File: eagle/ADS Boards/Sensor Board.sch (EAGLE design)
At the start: 15 parts

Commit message: Finish Preliminary Board Layouts
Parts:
- added H1, H2, H3, H4: MOUNT-HOLE3.0, holes:MOUNT-HOLE3.0
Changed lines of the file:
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@@
 <attribute name="DESIGNER" value="Yichen Xu"/>
 </part>
+<part name="H1" library="holes" library_urn="urn:adsk.eagle:library:237" deviceset="MOUNT-HOLE" device="3.0" package3d_urn="urn:adsk.eagle:package:14277/1"/>
+<part name="H2" library="holes" library_urn="urn:adsk.eagle:library:237" deviceset="MOUNT-HOLE" device="3.0" package3d_urn="urn:adsk.eagle:package:14277/1"/>
+<part name="H3" library="holes" library_urn="urn:adsk.eagle:library:237" deviceset="MOUNT-HOLE" device="3.0" package3d_urn="urn:adsk.eagle:package:14277/1"/>
+<part name="H4" library="holes" library_urn="urn:adsk.eagle:library:237" deviceset="MOUNT-HOLE" device="3.0" package3d_urn="urn:adsk.eagle:package:14277/1"/>
 </parts>
 <sheets>
@@
 <attribute name="CREVISION" x="234.92" y="1.17" size="2.54" layer="94" font="vector"/>
 </instance>
+<instance part="H1" gate="G$1" x="226.06" y="144.78" smashed="yes">
+<attribute name="NAME" x="228.092" y="145.3642" size="1.778" layer="95"/>
+<attribute name="VALUE" x="228.092" y="142.3162" size="1.778" layer="96"/>
+</instance>
+<instance part="H2" gate="G$1" x="226.06" y="137.16" smashed="yes">
+<attribute name="NAME" x="228.092" y="137.7442" size="1.778" layer="95"/>
+<attribute name="VALUE" x="228.092" y="134.6962" size="1.778" layer="96"/>
+</instance>
+<instance part="H3" gate="G$1" x="226.06" y="129.54" smashed="yes">
+<attribute name="NAME" x="228.092" y="130.1242" size="1.778" layer="95"/>
+<attribute name="VALUE" x="228.092" y="127.0762" size="1.778" layer="96"/>
+</instance>
+<instance part="H4" gate="G$1" x="226.06" y="121.92" smashed="yes">
+<attribute name="NAME" x="228.092" y="122.5042" size="1.778" layer="95"/>
+<attribute name="VALUE" x="228.092" y="119.4562" size="1.778" layer="96"/>
+</instance>
 </instances>

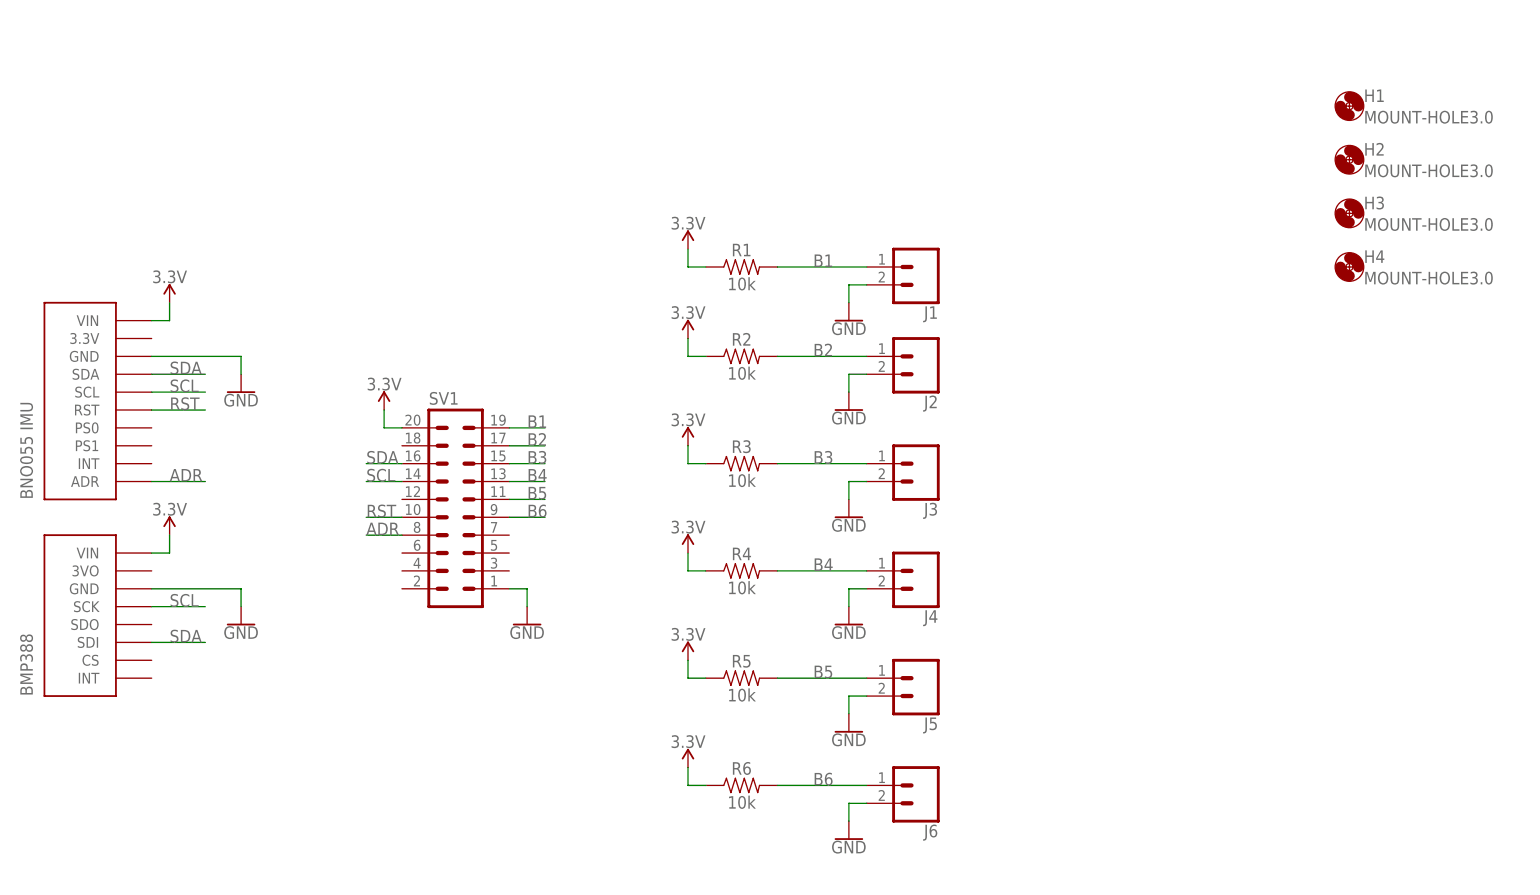
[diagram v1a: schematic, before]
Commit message: Modify to surface mount components
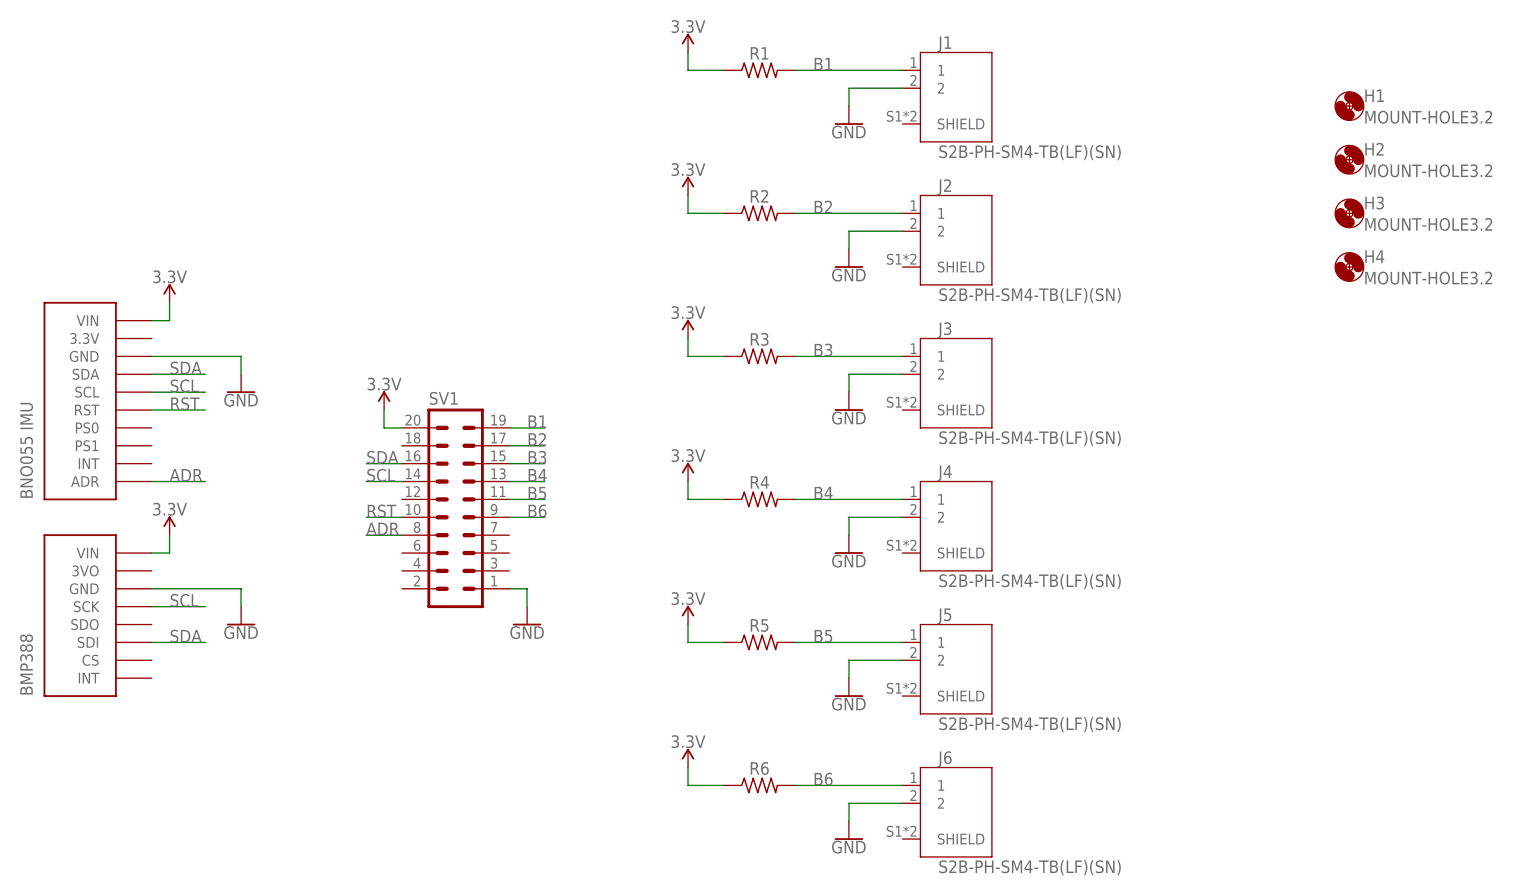
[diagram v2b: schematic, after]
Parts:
- H1, H2, H3, H4: value MOUNT-HOLE3.0 -> MOUNT-HOLE3.2; device holes:MOUNT-HOLE3.0 -> holes:MOUNT-HOLE3.2
- J1, J2, J3, J4, J5, J6: value (none) -> S2B-PH-SM4-TB(LF)(SN); device SparkFun-Connectors:CONN_02JST-PTH-2 -> S2B-PH-SM4-TB_LF__SN_:S2B-PH-SM4-TB(LF)(SN)
- R1, R2, R3, R4, R5, R6: device SparkFun-Resistors:10KOHM-HORIZ-1/4W-1% -> resistor:R-US_M1206
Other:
- moved on the sheet: R1, R2, R3, R4, R5, R6

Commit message: Finalized Boards, Gerbers, and DXF files.
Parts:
- removed SV1: (no value), con-lstb:MA10-2
- added J7: 62674-121121ALF, NUSTARS ADS Library:62674-121121ALF
- R1, R2, R3, R4, R5, R6: device resistor:R-US_M1206 -> resistor:R-US_R0805
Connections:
- net 3.3V: now also J7.11; no longer SV1.20
- net ADR: now also J7.1111; no longer SV1.8
- net B1: now also J7.44; no longer SV1.19
- net B2: now also J7.55; no longer SV1.17
- net B3: now also J7.66; no longer SV1.15
- net B4: now also J7.77; no longer SV1.13
- net B5: now also J7.88; no longer SV1.11
- net B6: now also J7.99; no longer SV1.9
- net GND: now also J7.1212; no longer SV1.1
- net RST: now also J7.1010; no longer SV1.10
- net SCL: now also J7.33; no longer SV1.14
- net SDA: now also J7.22; no longer SV1.16

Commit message: fixed rocket boards
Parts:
- removed J5, J6: S2B-PH-SM4-TB(LF)(SN), S2B-PH-SM4-TB_LF__SN_:S2B-PH-SM4-TB(LF)(SN)
- removed R3, R4, R5, R6: 10k, resistor:R-US_R0805
- J3: value S2B-PH-SM4-TB(LF)(SN) -> (none); device S2B-PH-SM4-TB_LF__SN_:S2B-PH-SM4-TB(LF)(SN) -> SparkFun-Connectors:CONN_08"
- J4: value S2B-PH-SM4-TB(LF)(SN) -> (none); device S2B-PH-SM4-TB_LF__SN_:S2B-PH-SM4-TB(LF)(SN) -> SparkFun-Connectors:CONN_06SILK_FEMALE_PTH
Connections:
- removed net B3: J3.1, J7.66, R3.2
- removed net B4: J4.1, J7.77, R4.2
- removed net B5: J5.1, J7.88, R5.2
- removed net B6: J6.1, J7.99, R6.2
- new net S0: J3.4, J4.2
- new net S1: J3.5, J4.3
- new net S2: J3.6, J4.4
- new net S3: J3.7, J4.5
- net 3.3V: now also J3.1, J4.1; no longer R3.1, R4.1, R5.1, R6.1
- net GND: now also J3.8, J4.6; no longer J3.2, J4.2, J5.2, J6.2
- net SCL: now also J3.3
- net SDA: now also J3.2
